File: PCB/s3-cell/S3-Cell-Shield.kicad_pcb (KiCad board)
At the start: 4 copper layers, 91 x 36 mm, 1 part, among them J6 DF40C-2x10 (stack)

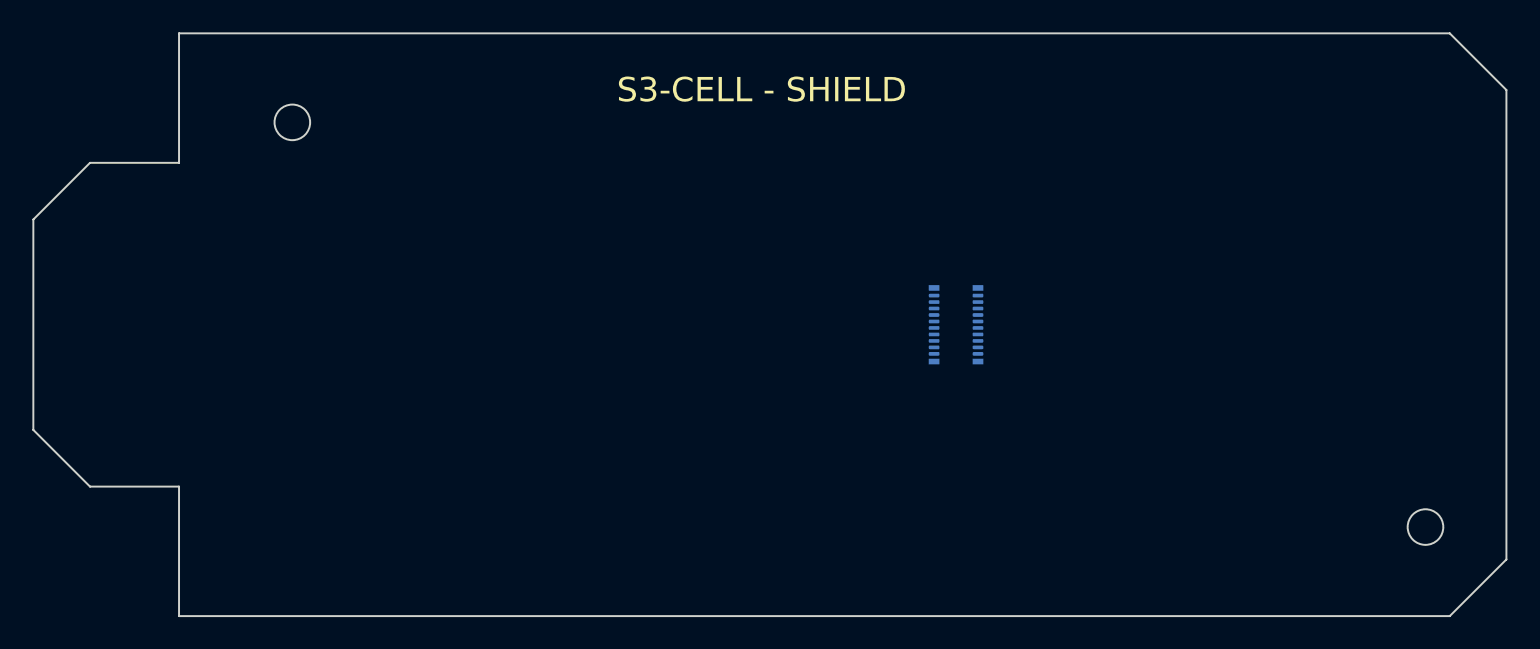
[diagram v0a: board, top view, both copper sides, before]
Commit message: Shield: populate with ESP32-C5 WiFi brain, 0.96" OLED, 3V3 LDO rail
- ESP32-C5-WROOM-1 (2.4/5 GHz Wi-Fi + BLE), PCB antenna facing the top
  edge (sideways, away from the west USB-C plug and the east cell/GPS SMAs)
- 0.96" I2C OLED (128x64, SSD1306) at the west for the UI
- Dedicated AP2112 3V3 LDO rail off VBAT with input/output bulk + module
  decoupling, EN/BOOT strapping
- I2C pull-ups for the display

Major components placed and overlap-free; net/route still to come.
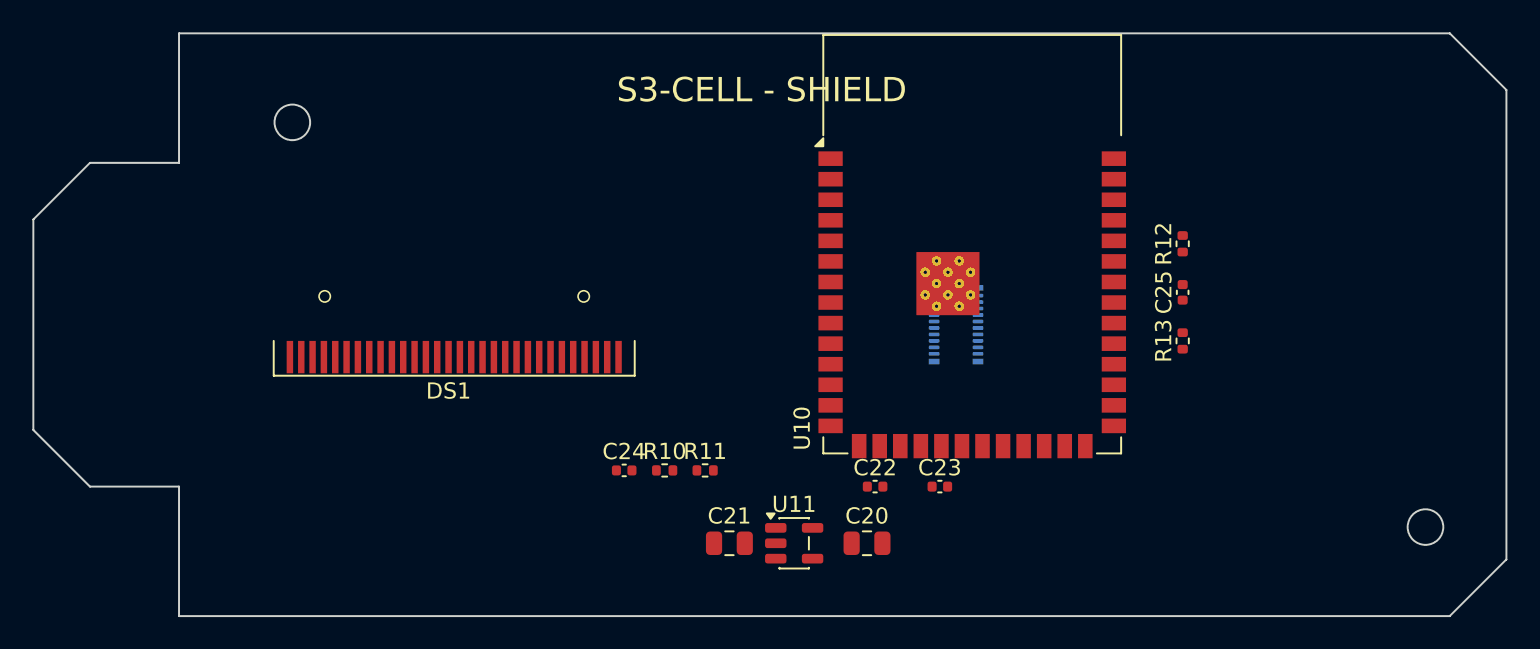
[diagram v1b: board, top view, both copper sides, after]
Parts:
- added C20: 10uF, C_0805_2012Metric, F.Cu at (151.5, 131.5)
- added C21: 10uF, C_0805_2012Metric, F.Cu at (143.0, 131.5)
- added C22: 100nF, C_0402_1005Metric, F.Cu at (152.0, 128.0)
- added C23: 100nF, C_0402_1005Metric, F.Cu at (156.0, 128.0)
- added C24: 100nF, C_0402_1005Metric, F.Cu at (136.5, 127.0)
- added C25: 100nF, C_0402_1005Metric, F.Cu at (171.0, 116.0)
- added DS1: OLED 0.96" I2C, OLED-128O064D, F.Cu at (126.0, 120.0)
- added R10: 4.7k, R_0402_1005Metric, F.Cu at (139.0, 127.0)
- added R11: 4.7k, R_0402_1005Metric, F.Cu at (141.5, 127.0)
- added R12: 10k, R_0402_1005Metric, F.Cu at (171.0, 113.0)
- added R13: 10k, R_0402_1005Metric, F.Cu at (171.0, 119.0)
- added U10: ESP32-C5-WROOM-1, ESP32-S3-WROOM-1, F.Cu at (158.0, 113.0)
- added U11: AP2112-3.3, SOT-23-5, F.Cu at (147.0, 131.5)

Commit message: Shield UI: 1.14" colour TFT + 5-button D-pad; relocate a mounting hole
- Swap the 0.96" OLED for a 1.14" ST7789 colour IPS TFT (SPI) - represented
  by its 12-pin 0.5mm FPC connector plus a glass outline; drop the I2C
  pull-ups (no longer needed)
- Add a D-pad next to the screen: up / down / left / right + centre Select
  (B3U-1000P low-profile tacts), matching the reference layout
- Shift the ESP32-C5 module to the east end (antenna still north) to make
  room for the bigger screen and the buttons
- Move the second mounting hole off the packed east end (it landed 1.2 mm
  from the GNSS SMA and over the back-side SIM) to centre-north by the stack
  connector; both boards keep identical, aligned hole positions

Placement verified overlap-free on both sides; holes >=4mm from all pads.
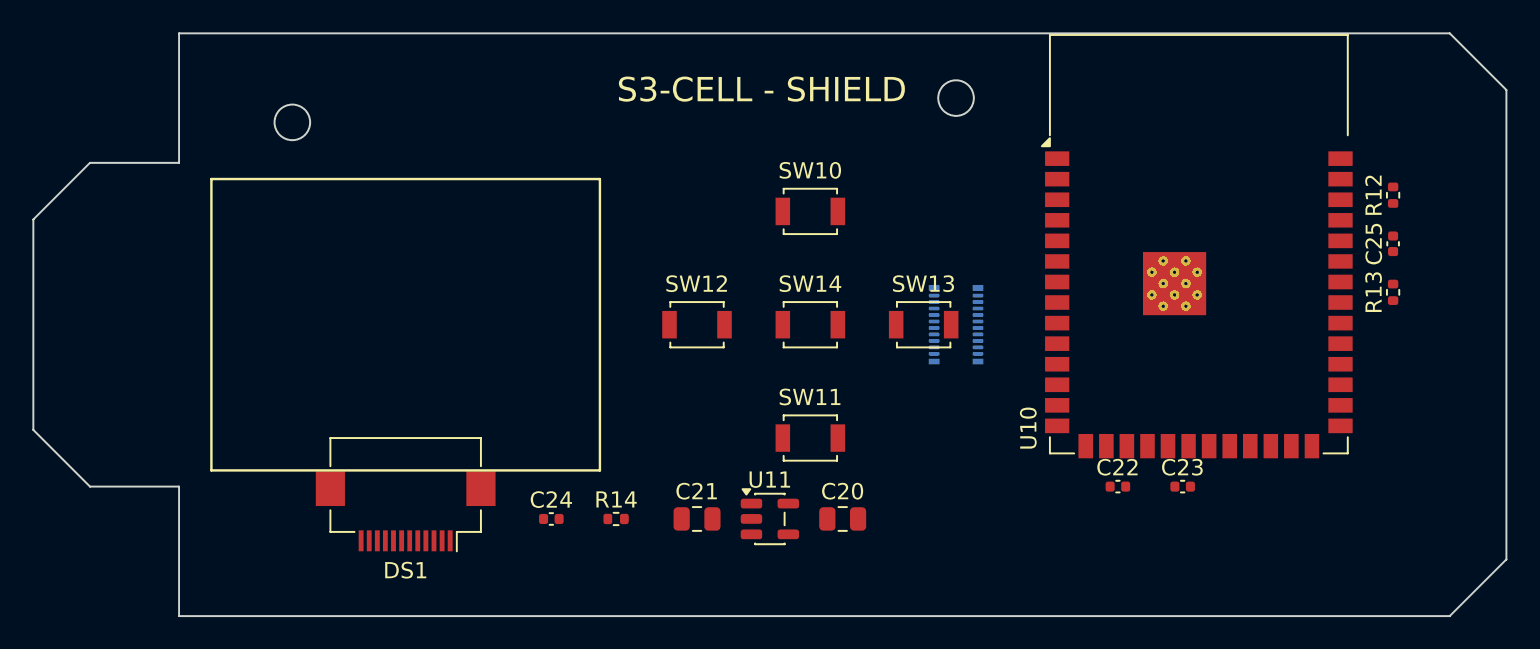
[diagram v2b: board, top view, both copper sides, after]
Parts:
- removed R10, R11: 4.7k, R_0402_1005Metric
- added R14: BL 10R, R_0402_1005Metric, F.Cu at (136.0, 130.0)
- added SW10: UP, SW_SPST_B3U-1000P, F.Cu at (148.0, 111.0)
- added SW11: DOWN, SW_SPST_B3U-1000P, F.Cu at (148.0, 125.0)
- added SW12: LEFT, SW_SPST_B3U-1000P, F.Cu at (141.0, 118.0)
- added SW13: RIGHT, SW_SPST_B3U-1000P, F.Cu at (155.0, 118.0)
- added SW14: SEL, SW_SPST_B3U-1000P, F.Cu at (148.0, 118.0)
- DS1: value OLED 0.96" I2C -> TFT 1.14" ST7789; footprint OLED-128O064D -> Hirose_FH12-12S-0.5SH_1x12-1MP_P0.50mm_Horizontal
- moved C22 15.0 mm to (167.0, 128.0)
- moved C23 15.0 mm to (171.0, 128.0)
- moved U10 14.0 mm to (172.0, 113.0)
- moved C25 13.3 mm to (184.0, 113.0)
- moved R12 13.3 mm to (184.0, 110.0)
- moved R13 13.3 mm to (184.0, 116.0)
- moved DS1 9.96 mm to (123.0, 129.5), turned to 180 degrees
- moved C24 5.41 mm to (132.0, 130.0)
- moved C21 2.50 mm to (141.0, 130.0)
- moved C20 2.12 mm to (150.0, 130.0)
- moved U11 2.12 mm to (145.5, 130.0)
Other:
- outline, holes or cut-outs redrawn
